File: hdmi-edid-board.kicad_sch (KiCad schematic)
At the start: 82 parts, among them J1 HDMI-A_WE_685119134923, J4 HDMI-A_WE_685119134923, J5 USB-C_GCT_USB4105-GF-A, J6 JST_SH_1x4_SM04B-SRSS-TB-LF-SN, J7 PinHeader_2x3_P2.54mm_Drill1.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, U1 24LC02BT-I/SN, U2 24AA024T-I/SN, U3 NTS0302JKZ, U4 TLV70033_SC70, U5 FT4232H_VQFN, U6 TPS2117DRLR, Y1 Oscillator_12MHz_ASFLMB

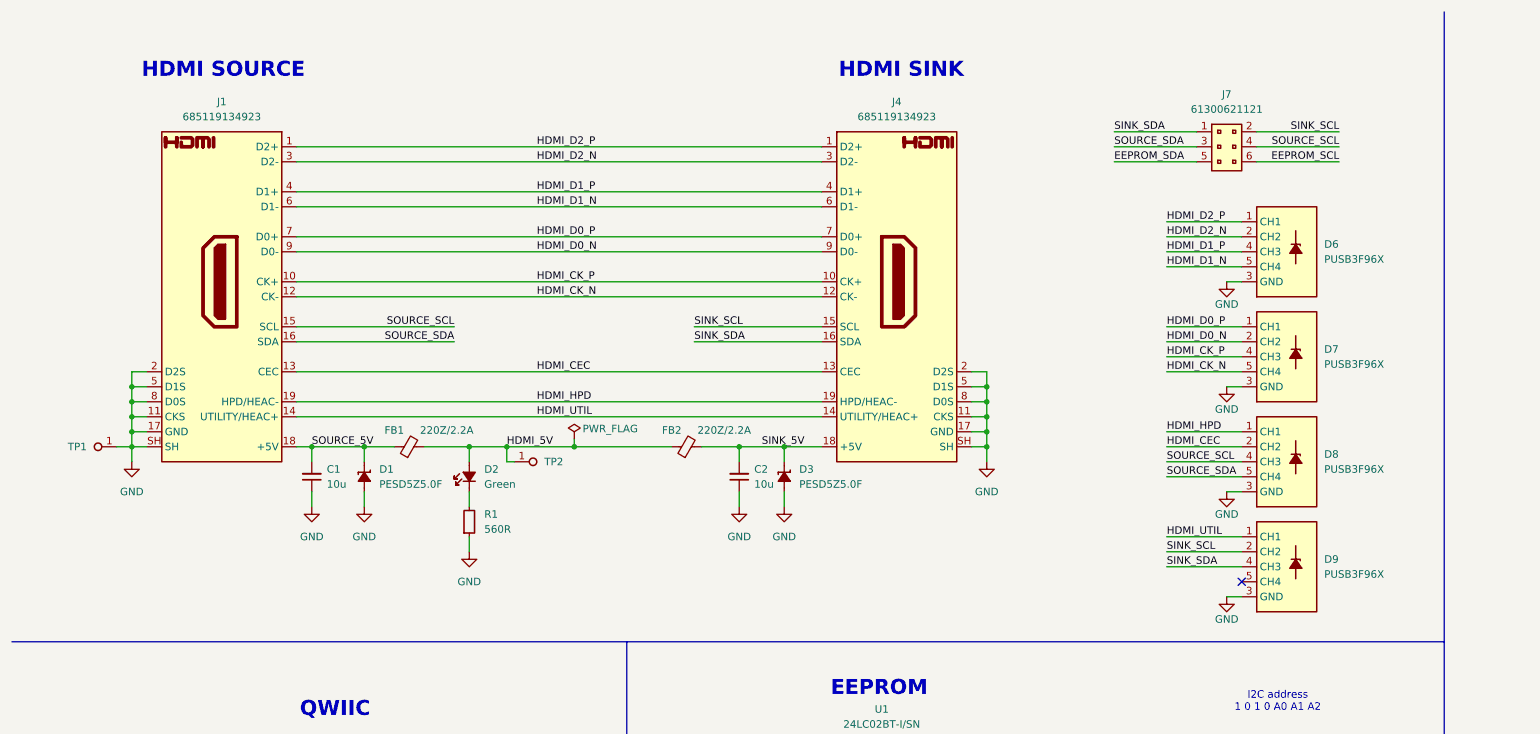
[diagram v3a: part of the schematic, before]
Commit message: [#77357] Route HDMI and USB
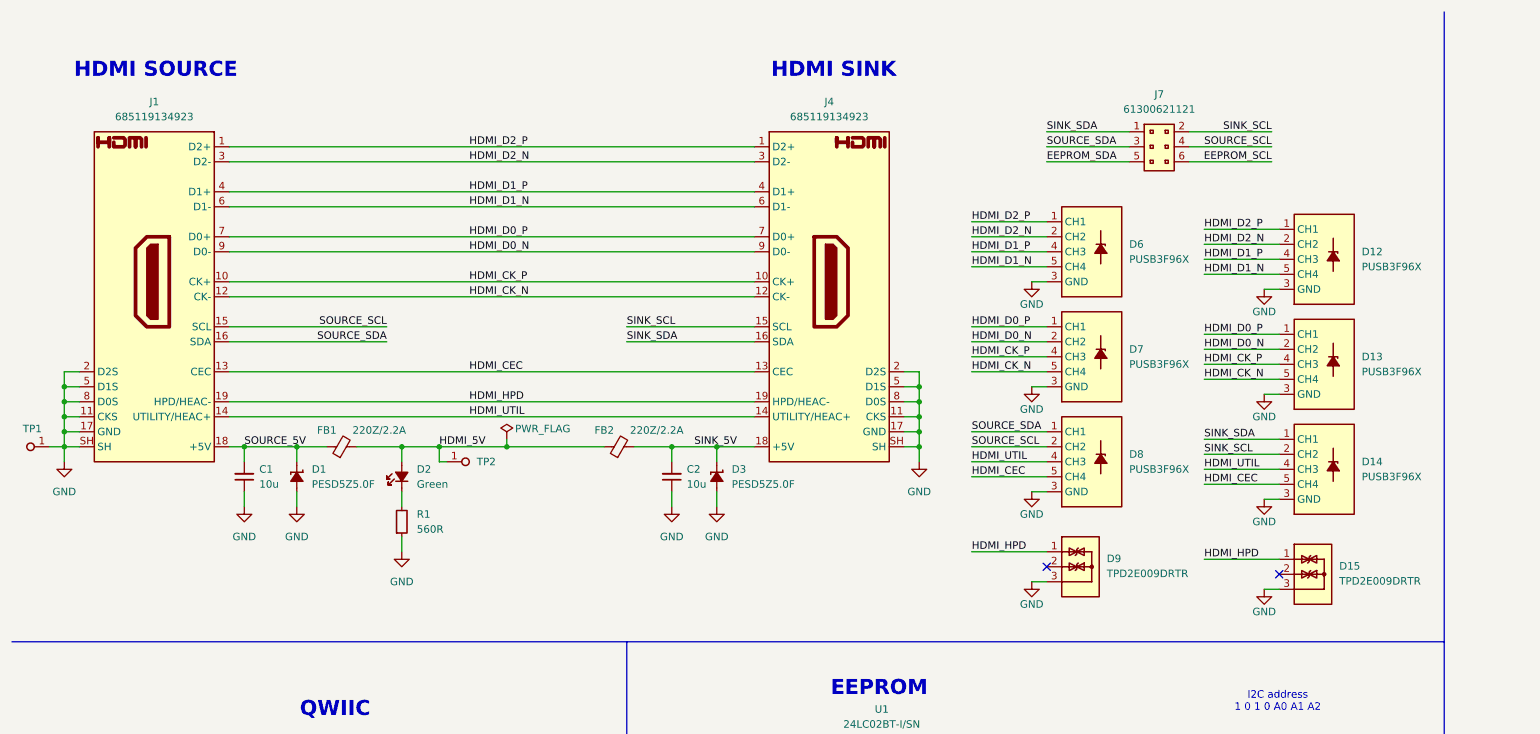
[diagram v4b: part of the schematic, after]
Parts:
- removed D9: PUSB3F96X_PASS, antmicro-footprints:Nexperia_DFN-10_2.5x1mm_P0.5mm, symbol antmicroTVSDiodes:PUSB3F96X_PASS
- added D12, D13, D14: PUSB3F96X_PASS, antmicro-footprints:Nexperia_DFN-10_2.5x1mm_P0.5mm, symbol antmicroTVSDiodes:PUSB3F96X_PASS
- added D15, D9: TPD2E009_SOT-9X3, antmicro-footprints:SOT-723, symbol antmicroTVSDiodes:TPD2E009_SOT-9X3
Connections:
- net GND: now also D12.3 (GND), D12.8 (GND), D13.3 (GND), D13.8 (GND), D14.3 (GND), D14.8 (GND), D15.3, D9.3
- net HDMI_CEC: now also D8.5 (CH4), D8.6 (CH4), D14.5 (CH4), D14.6 (CH4); no longer D8.2 (CH2), D8.9 (CH2)
- net HDMI_CK_N: now also D13.5 (CH4), D13.6 (CH4)
- net HDMI_CK_P: now also D13.4 (CH3), D13.7 (CH3)
- net HDMI_D0_N: now also D13.2 (CH2), D13.9 (CH2)
- net HDMI_D0_P: now also D13.1 (CH1), D13.10 (CH1)
- net HDMI_D1_N: now also D12.5 (CH4), D12.6 (CH4)
- net HDMI_D1_P: now also D12.4 (CH3), D12.7 (CH3)
- net HDMI_D2_N: now also D12.2 (CH2), D12.9 (CH2)
- net HDMI_D2_P: now also D12.1 (CH1), D12.10 (CH1)
- net HDMI_HPD: now also D15.1, D9.1; no longer D8.1 (CH1), D8.10 (CH1)
- net HDMI_UTIL: now also D8.4 (CH3), D8.7 (CH3), D14.4 (CH3), D14.7 (CH3)
- net SINK_SCL: now also D14.2 (CH2), D14.9 (CH2)
- net SINK_SDA: now also D14.1 (CH1), D14.10 (CH1)
- net SOURCE_SCL: now also D8.2 (CH2), D8.9 (CH2); no longer D8.4 (CH3), D8.7 (CH3)
- net SOURCE_SDA: now also D8.1 (CH1), D8.10 (CH1); no longer D8.5 (CH4), D8.6 (CH4)
- no-connect marks 39 -> 40
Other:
- moved on the sheet: C1, C2, D1, D2, D3, D6, D7, D8, FB1, FB2, J1, J4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

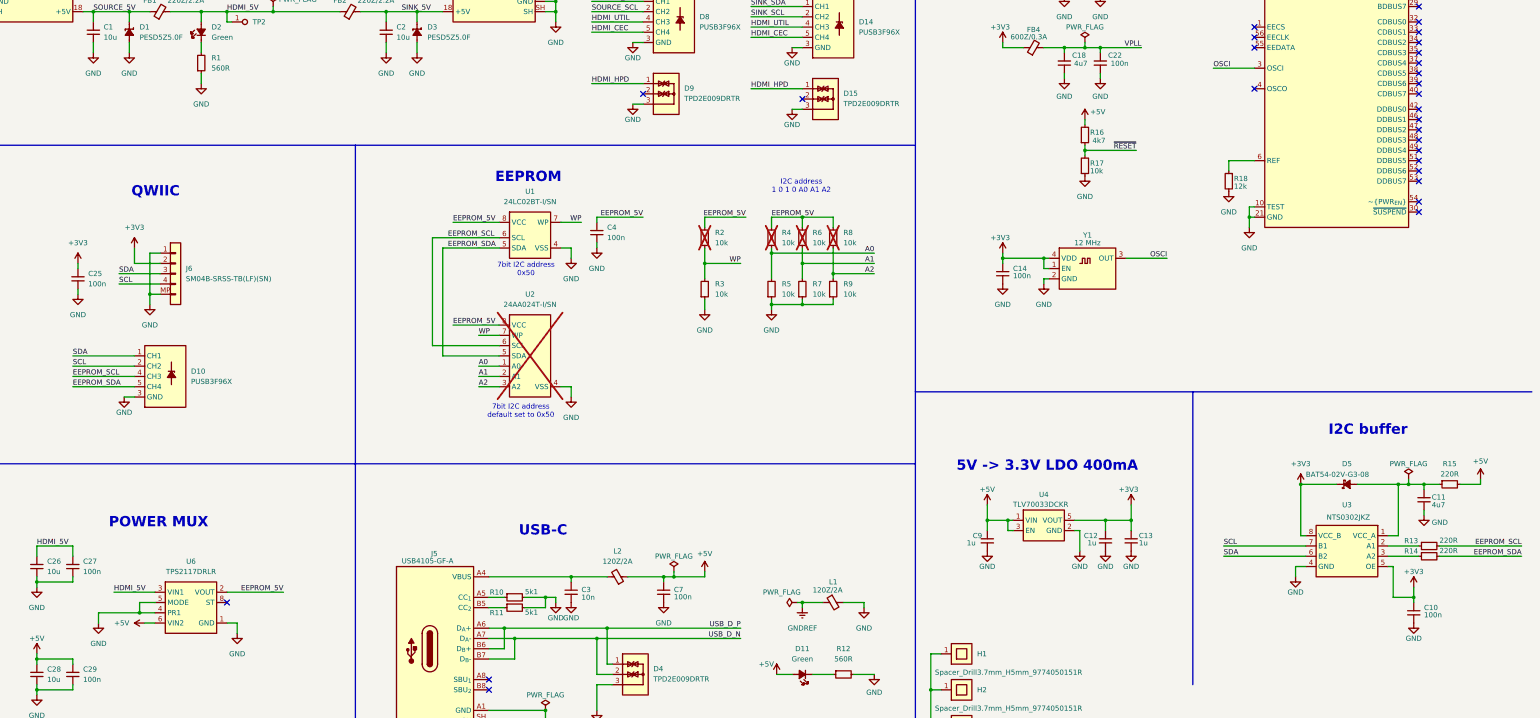
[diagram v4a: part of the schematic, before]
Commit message: [#77357] Route remaining connections
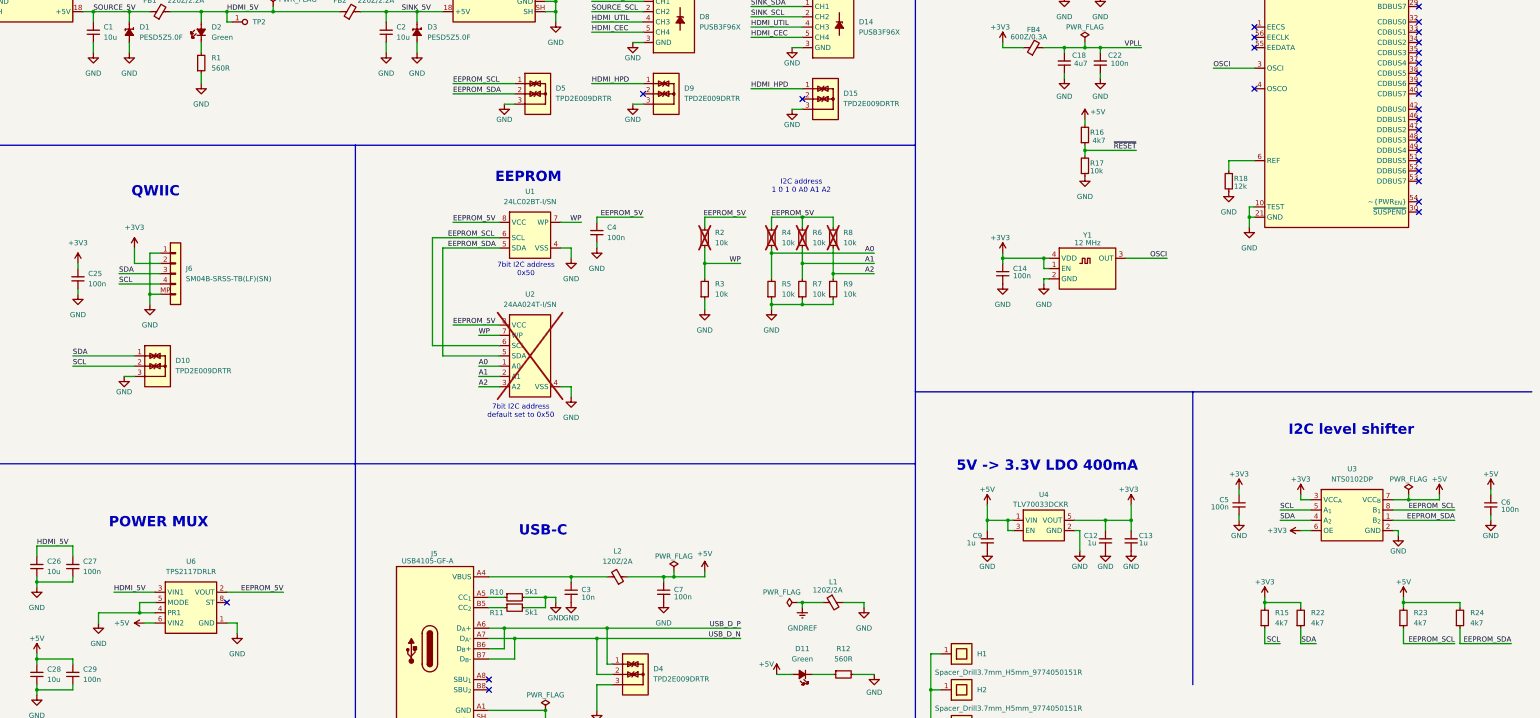
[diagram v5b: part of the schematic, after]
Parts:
- removed C10: C_100n_16V_X7R_0402, antmicro-footprints:C_0402_1005Metric, symbol antmicroCapacitors0402:C_100n_16V_X7R_0402
- removed C11: C_4u7_0402, antmicro-footprints:C_0402_1005Metric, symbol antmicroCapacitors0402:C_4u7_0402
- removed D10: PUSB3F96X_PASS, antmicro-footprints:Nexperia_DFN-10_2.5x1mm_P0.5mm, symbol antmicroTVSDiodes:PUSB3F96X_PASS
- removed D5: BAT54-02V-G3-08, antmicro-footprints:SOD-523, symbol antmicroDiodesRectifiersSingle:BAT54-02V-G3-08
- removed R13, R14, R15: R_220R_0402, antmicro-footprints:R_0402_1005Metric, symbol antmicroResistors0402:R_220R_0402
- removed U3: NTS0302JKZ, antmicro-footprints:X2SON8_1.4x1x0.32mm_P0.35mm, symbol antmicroLogicTranslatorsLevelShifters:NTS0302JKZ
- added C5, C6: C_100n_16V_X7R_0402, antmicro-footprints:C_0402_1005Metric, symbol antmicroCapacitors0402:C_100n_16V_X7R_0402
- added D10, D5: TPD2E009_SOT-9X3, antmicro-footprints:SOT-723, symbol antmicroTVSDiodes:TPD2E009_SOT-9X3
- added R15, R22, R23, R24: R_4k7_0402, antmicro-footprints:R_0402_1005Metric, symbol antmicroResistors0402:R_4k7_0402
- added U3: NTS0102_TSSOP, antmicro-footprints:TSSOP-8_3x3mm_P0.65mm, symbol antmicroLogicTranslatorsLevelShifters:NTS0102_TSSOP
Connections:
- net +3V3: now also C5.1, R15.2, R22.2, U3.3 (VCC_{A}), U3.6 (OE)
- net +5V: now also C6.1, R23.2, R24.2, U3.7 (VCC_{B})
- net EEPROM_SCL: now also D5.1, R23.1, U3.8 (B_{1})
- net EEPROM_SDA: now also D5.2, R24.1, U3.1 (B_{2})
- net GND: now also C5.2, C6.2, D10.3, D5.3, U3.2 (GND)
- net SCL: now also D10.2, R15.1, U3.5 (A_{1})
- net SDA: now also D10.1, R22.1, U3.4 (A_{2})
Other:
- note added: "I2C level shifter"
- note removed: "I2C buffer"
